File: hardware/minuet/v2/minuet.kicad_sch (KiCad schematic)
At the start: 38 parts, among them J101 B2P-VH-B, J102 B2B-XH-A, J103 PPPC062LFBN-RC, J104 B2B-XH-A, Q101 MMBT3904, U101 TSOP39238, U102 LMV331X-SC5R

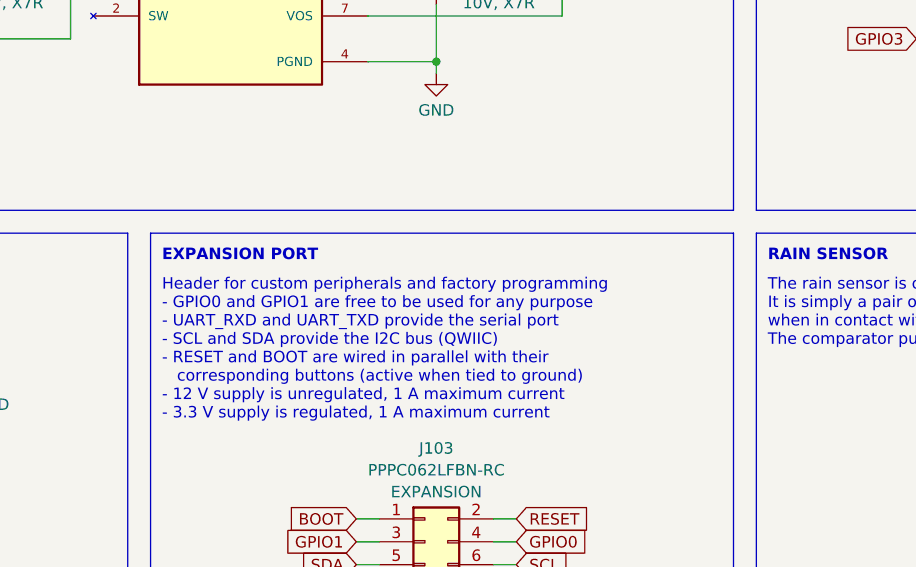
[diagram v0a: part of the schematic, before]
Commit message: Wordsmithing accessories and components.
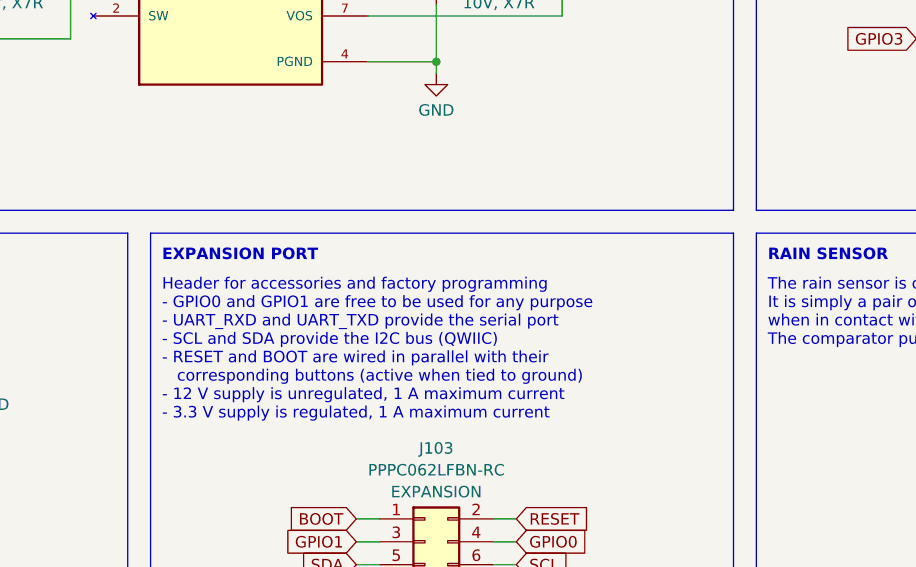
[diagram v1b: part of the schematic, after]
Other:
- note added: "Header for accessories and factory programming - GPIO0 and GPIO1 are free to be used for any purpose - UART_RXD and UART_TXD provide the serial port - SCL and SDA provide the I2C bus (QWIIC) - RESET and BOOT are wired in parallel with their corresponding buttons (active when tied to ground) - 12 V supply is unregulated, 1 A maximum current - 3.3 V supply is regulated, 1 A maximum current"
- note removed: "Header for custom peripherals and factory programming - GPIO0 and GPIO1 are free to be used for any purpose - UART_RXD and UART_TXD provide the serial port - SCL and SDA provide the I2C bus (QWIIC) - RESET and BOOT are wired in parallel with their corresponding buttons (active when tied to ground) - 12 V supply is unregulated, 1 A maximum current - 3.3 V supply is regulated, 1 A maximum current"
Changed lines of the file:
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@@
 		)
 	)
-	(text "Header for custom peripherals and factory programming\n- GPIO0 and GPIO1 are free to be used for any purpose\n- UART_RXD and UART_TXD provide the serial port\n- SCL and SDA provide the I2C bus (QWIIC)\n- RESET and BOOT are wired in parallel with their\n   corresponding buttons (active when tied to ground)\n- 12 V supply is unregulated, 1 A maximum current\n- 3.3 V supply is regulated, 1 A maximum current"
+	(text "Header for accessories and factory programming\n- GPIO0 and GPIO1 are free to be used for any purpose\n- UART_RXD and UART_TXD provide the serial port\n- SCL and SDA provide the I2C bus (QWIIC)\n- RESET and BOOT are wired in parallel with their\n   corresponding buttons (active when tied to ground)\n- 12 V supply is unregulated, 1 A maximum current\n- 3.3 V supply is regulated, 1 A maximum current"
 		(exclude_from_sim no)
 		(at 82.55 92.71 0)

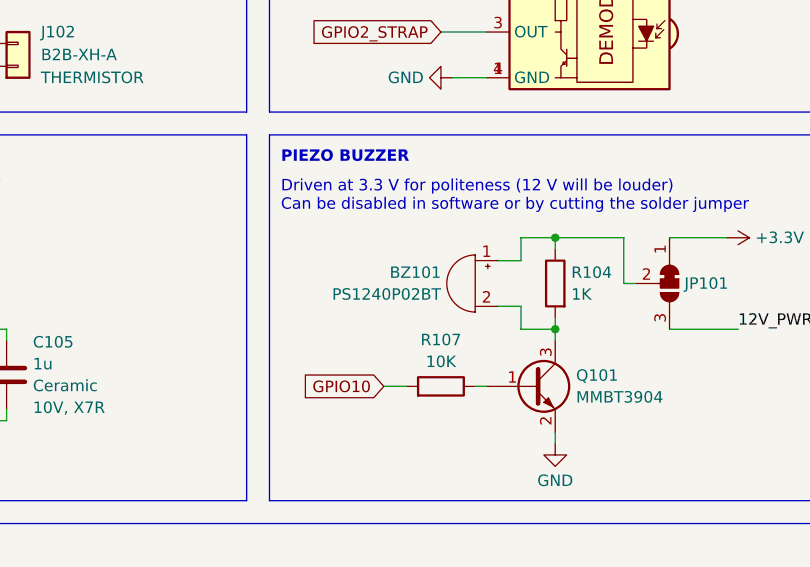
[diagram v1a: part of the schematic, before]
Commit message: Make the piezo buzzer symbol unpolarized.
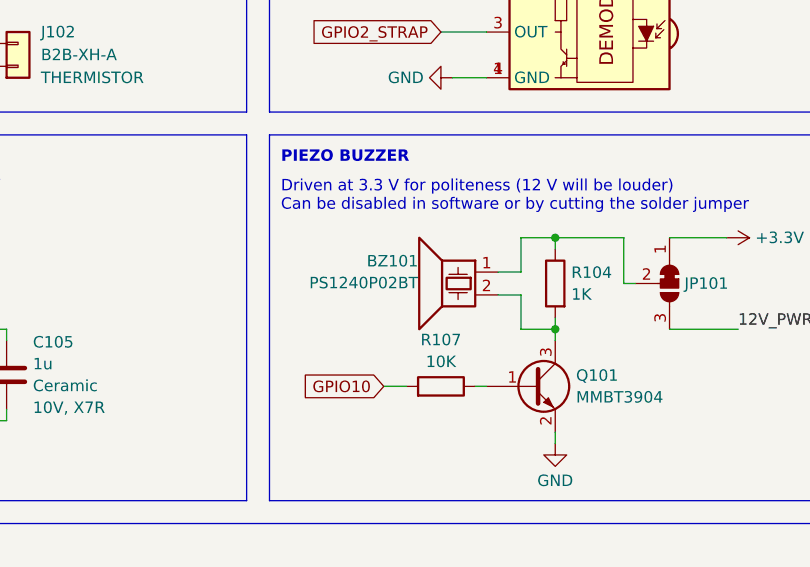
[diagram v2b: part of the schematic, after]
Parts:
- BZ101: symbol Device:Buzzer -> Device:Speaker_Crystal
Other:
- company: (none) -> Brown Studios LLC
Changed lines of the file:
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@@
 		(date "2025-02")
 		(rev "2.0")
+		(company "Brown Studios LLC")
 	)
 	(junction
@@
 	(wire
 		(pts
+			(xy 241.3 59.69) (xy 243.84 59.69)
+		)
+		(stroke
+			(width 0)
+			(type default)
+		)
+	)
+	(wire
+		(pts
 			(xy 72.39 58.42) (xy 72.39 66.04)
 		)
@@
 	(wire
 		(pts
-			(xy 243.84 58.42) (xy 243.84 55.88)
+			(xy 243.84 55.88) (xy 243.84 59.69)
 		)
 		(stroke
@@
 	(wire
 		(pts
-			(xy 241.3 63.5) (xy 243.84 63.5)
-		)
-		(stroke
-			(width 0)
-			(type default)
-		)
-	)
-	(wire
-		(pts
 			(xy 58.42 53.34) (xy 74.93 53.34)
 		)
@@
 	(wire
 		(pts
-			(xy 243.84 63.5) (xy 243.84 66.04)
-		)
-		(stroke
-			(width 0)
-			(type default)
-		)
-	)
-	(wire
-		(pts
 			(xy 33.02 165.1) (xy 45.72 165.1)
 		)
@@
 	(wire
 		(pts
-			(xy 241.3 58.42) (xy 243.84 58.42)
-		)
-		(stroke
-			(width 0)
-			(type default)
-		)
-	)
-	(wire
-		(pts
 			(xy 26.67 53.34) (xy 29.21 53.34)
 		)
@@
 	(wire
 		(pts
+			(xy 243.84 62.23) (xy 243.84 66.04)
+		)
+		(stroke
+			(width 0)
+			(type default)
+		)
+	)
+	(wire
+		(pts
 			(xy 207.01 127) (xy 207.01 128.27)
 		)
@@
 		(pts
 			(xy 33.02 160.02) (xy 45.72 160.02)
+		)
+		(stroke
+			(width 0)
+			(type default)
+		)
+	)
+	(wire
+		(pts
+			(xy 241.3 62.23) (xy 243.84 62.23)
 		)
 		(stroke
@@
 	)
 	(symbol
-		(lib_id "Device:Buzzer")
-		(at 238.76 60.96 0)
+		(lib_id "Device:Speaker_Crystal")
+		(at 236.22 59.69 0)
 		(mirror y)
 		(unit 1)
@@
 		(dnp no)
 		(property "Reference" "BZ101"
-			(at 234.9638 59.7478 0)
+			(at 232.4238 58.4778 0)
 			(effects
 				(font
@@
 		)
 		(property "Value" "PS1240P02BT"
-			(at 234.9638 62.1721 0)
+			(at 232.4238 60.9021 0)
 			(effects
 				(font
@@
 		)
 		(property "Footprint" "Buzzer_Beeper:Buzzer_TDK_PS1240P02BT_D12.2mm_H6.5mm"
-			(at 239.395 58.42 90)
+			(at 236.855 57.15 90)
 			(effects
 				(font
@@
 		)
 		(property "Datasheet" "https://product.tdk.com/en/system/files/dam/doc/product/sw_piezo/sw_piezo/piezo-buzzer/catalog/piezoelectronic_buzzer_ps_en.pdf"
-			(at 239.395 58.42 90)
-			(effects
-				(font
-					(size 1.27 1.27)
-				)
-				(hide yes)
-			)
-		)
-		(property "Description" "Buzzer, polarized"
-			(at 238.76 60.96 0)
-			(effects
-				(font
+			(at 236.855 57.15 90)
+			(effects
+				(font
+					(size 1.27 1.27)
+				)
+				(hide yes)
+			)
+		)
+		(property "Description" "Piezo buzzer"
+			(at 236.22 59.69 0)
+			(effects
+				(font

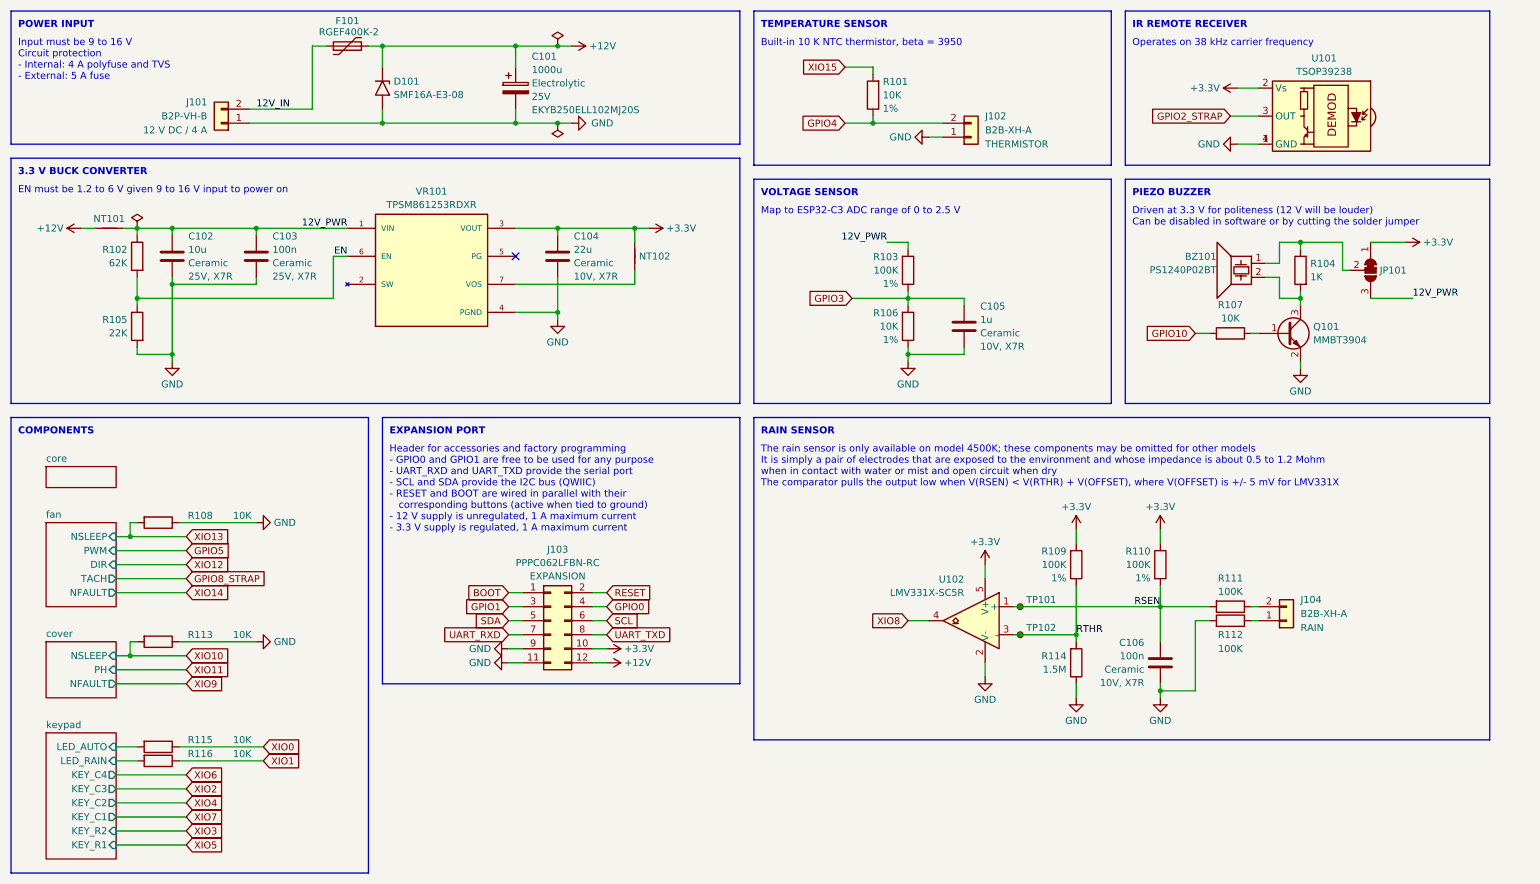
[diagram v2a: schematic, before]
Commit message: Finalize Minuet v2.1 for manufacture.
This revision uses a different motor controller and buck converter
and remedies errata from v2.0.
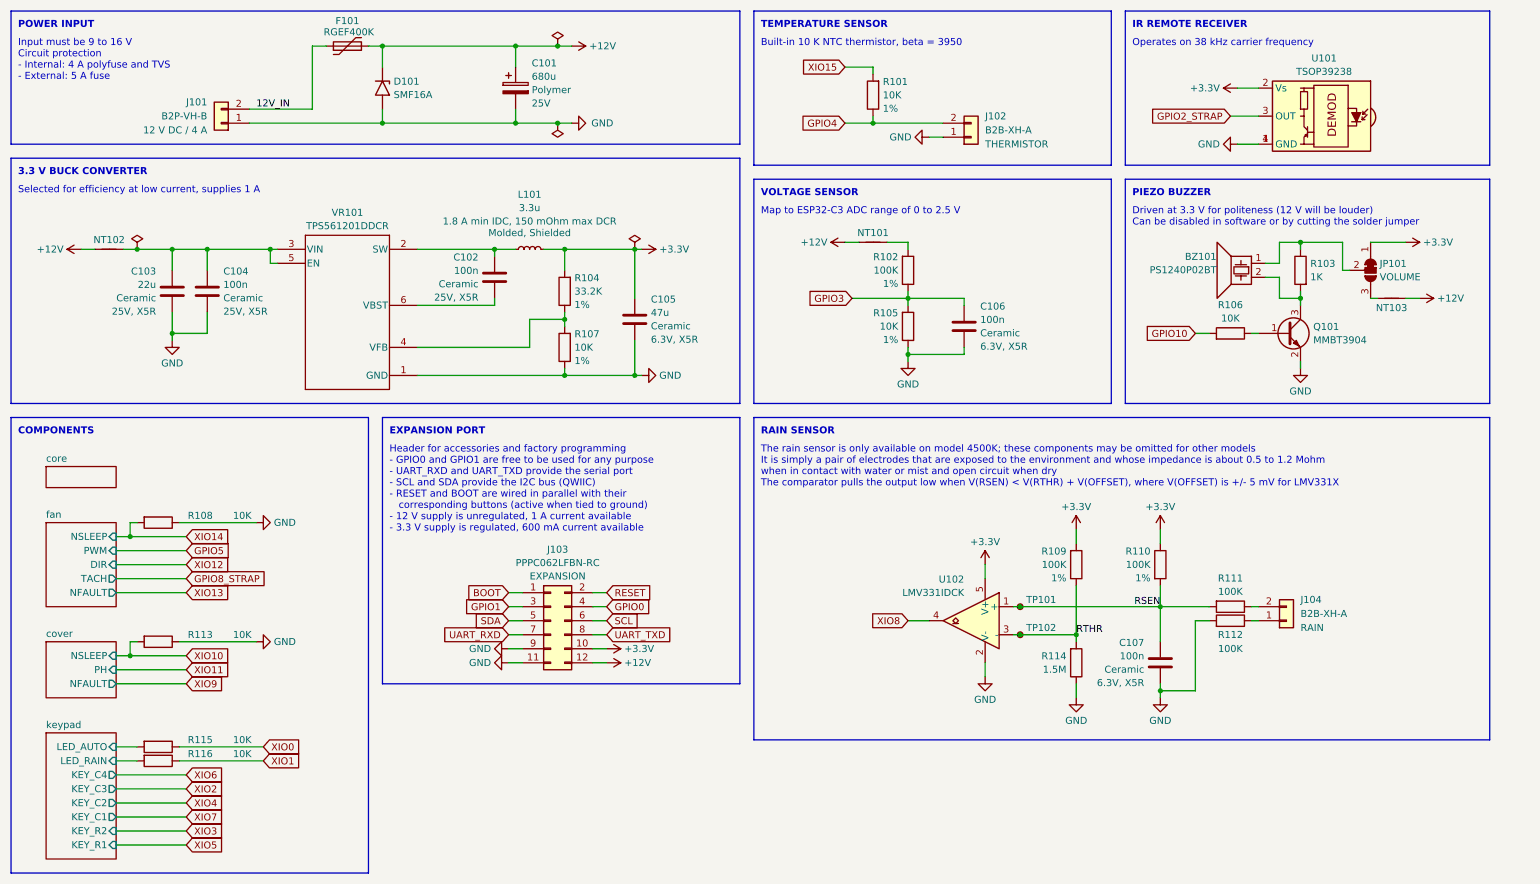
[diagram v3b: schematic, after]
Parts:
- removed NT102: NetTie_2, Generic:NetTie-2_SMD_Pad0.2mm, symbol Device:NetTie_2
- removed R102: 62K, Resistor_SMD:R_0603_1608Metric, symbol Device:R
- removed R105: 22K, Resistor_SMD:R_0603_1608Metric, symbol Device:R
- added C102: 100n, Capacitor_SMD:C_0603_1608Metric, symbol Device:C
- added L101: 3.3u, Inductor_SMD:L_1008_2520Metric, symbol Device:L_Small
- added NT101: NetTie_2, Generic:NetTie-2_SMD_Pad0.2mm, symbol Device:NetTie_2
- added NT103: NetTie_2, Generic:NetTie-2_SMD_Pad0.4mm, symbol Device:NetTie_2
- added R104: 33.2K, Resistor_SMD:R_0603_1608Metric, symbol Device:R
- added R107: 10K, Resistor_SMD:R_0603_1608Metric, symbol Device:R
- BZ101: LCSC (none) -> C76871
- C101: value 1000u -> 680u; footprint Capacitor_THT:CP_Radial_D10.0mm_P5.00mm -> Capacitor_THT:CP_Radial_D8.0mm_P3.50mm; LCSC (none) -> C1020064; Part EKYB250ELL102MJ20S -> A750KW687M1EAAE016; Type Electrolytic -> Polymer
- C103: renamed from C102; value 10u -> 22u; footprint Capacitor_SMD:C_1206_3216Metric -> Capacitor_SMD:C_0805_2012Metric; Rating 25V, X7R -> 25V, X5R
- C104: renamed from C103; Rating 25V, X7R -> 25V, X5R
- C105: renamed from C104; value 22u -> 47u; footprint Capacitor_SMD:C_1206_3216Metric -> Capacitor_SMD:C_0805_2012Metric; Rating 10V, X7R -> 6.3V, X5R
- C106: renamed from C105; value 1u -> 100n; Rating 10V, X7R -> 6.3V, X5R
- C107: renamed from C106; Rating 10V, X7R -> 6.3V, X5R
- D101: value SMF16A-E3-08 -> SMF16A; Alternative (none) -> SMF16A-E3-08; LCSC (none) -> C207257
- F101: value RGEF400K-2 -> RGEF400K; LCSC (none) -> C468987
- J101: LCSC (none) -> C265114
- J102, J104: LCSC (none) -> C158012
- J103: LCSC (none) -> C20071205
- JP101: Label (none) -> VOLUME
- Q101: LCSC (none) -> C239187
- U101: LCSC (none) -> C7128407
- U102: value LMV331X-SC5R -> LMV331IDCK; Alternative (none) -> LMV331X-SC5R; LCSC (none) -> C7976
- VR101: value TPSM861253RDXR -> TPS561201DDCR; footprint TPSM861253RDXR:VREG_TPSM861253RDXR -> TPS561201:SOT95P280X110-6N; symbol TPSM861253RDXR:TPSM861253RDXR -> TPS561201:TPS561201DDCR; Availability In Stock -> (none); Check_prices https://www.snapeda.com/parts/TPSM861253RDXR/Texas+Instrume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 -> (none); Description_1 3V to 17V input voltage, 3.3V, 1A output synchronous buck m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 -> (none); LCSC (none) -> C220433; MANUFACTURER Texas Instruments -> (none); MAXIMUM_PACKAGE_HEIGHT 2.1mm -> (none); MF Texas Instruments -> (none); MP TPSM861253RDXR -> (none); PARTREV B -> (none); Package PowerFQFN-7 Texas Instruments -> (none); Price None -> (none); STANDARD Manufacturer Recommendations -> (none); SnapEDA_Link https://www.snapeda.com/parts/TPSM861253RDXR/Texas+Instrume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 -> (none)
- renumbered NT101 to NT102, R103 to R102, R104 to R103, R106 to R105, R107 to R106
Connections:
- net +12V: now also NT101.1, NT103.1
- net +3.3V: now also L101.1, R104.2; no longer VR101.3 (VOUT)
- net GND: now also VR101.1 (GND), R107.1; no longer VR101.4 (PGND)
- net XIO13: no longer R108.2
- net XIO14: now also R108.2
- net at VR101.2 (SW): now also C102.1, L101.2
- net at VR101.5 (EN): now also C103.1, C104.1, NT102.2, VR101.3 (VIN)
- removed net 12V_PWR: C103.1, C104.1, JP101.3 (B), NT102.2, R102.2, VR101.1 (VIN)
- net EN: no longer names the net of VR101.6 (VBST)
- net EN: now also C102.2
- new net: JP101.3 (B), NT103.2
- new net: NT101.2, R102.2
- new net: R104.1, R107.2, VR101.4 (VFB)
- no-connect marks 1 -> 0
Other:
- note added: "Header for accessories and factory programming - GPIO0 and GPIO1 are free to be used for any purpose - UART_RXD and UART_TXD provide the serial port - SCL and SDA provide the I2C bus (QWIIC) - RESET and BOOT are wired in parallel with their corresponding buttons (active when tied to ground) - 12 V supply is unregulated, 1 A current available - 3.3 V supply is regulated, 600 mA current available"
- note added: "Selected for efficiency at low current, supplies 1 A"
- note removed: "EN must be 1.2 to 6 V given 9 to 16 V input to power on"
- note removed: "Header for accessories and factory programming - GPIO0 and GPIO1 are free to be used for any purpose - UART_RXD and UART_TXD provide the serial port - SCL and SDA provide the I2C bus (QWIIC) - RESET and BOOT are wired in parallel with their corresponding buttons (active when tied to ground) - 12 V supply is unregulated, 1 A maximum current - 3.3 V supply is regulated, 1 A maximum current"
- moved on the sheet: C103, C104, C105, NT102
